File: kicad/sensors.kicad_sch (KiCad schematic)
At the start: 18 parts, among them U10 W25N01GV, U6 ICM-42688-P, U7 BMI270, U8 BMP390, U9 IIS2MDC

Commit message: Gate 1 fixes (crystal gm evidence, LDO output ESR, X7R caps, 50V HF cap, per-MPN datasheets, in_bom flags, project-file merge, parity fields), power re-audit fixes (board-level thermal envelope, USB inrush deviation, R41 VTX 0R link), PCB placement + legalizer + grommet keepouts; Gate 1 reports
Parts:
- C39: value 2.2uF X5R 16V -> 2.2uF X7R 16V; DigiKey 1276-1183-1-ND (verify) -> 1276-1184-1-ND (verify); MPN CL10A225KO8NNNC -> CL10B225KO8NNNC
- C47: value 1uF X5R 25V -> 4.7uF X5R 16V; DigiKey 1276-1102-1-ND (verify) -> 1276-1044-1-ND (verify); MPN CL10A105KA8NNNC -> CL10A475KO8NNNC
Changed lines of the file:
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@@
 			)
 		)
-		(property "Datasheet" "https://product.samsungsem.com/mlcc/"
+		(property "Datasheet" "https://product.samsungsem.com/mlcc/CL05B104KO5NNNC.do"
 			(at 93.98 35.56 0)
 			(effects
@@
 			)
 		)
-		(property "Value" "2.2uF X5R 16V"
+		(property "Value" "2.2uF X7R 16V"
 			(at 119.38 41.91 0)
 			(effects
@@
 			)
 		)
-		(property "Datasheet" "https://product.samsungsem.com/mlcc/"
+		(property "Datasheet" "https://product.samsungsem.com/mlcc/CL10B225KO8NNNC.do"
 			(at 119.38 35.56 0)
 			(effects
@@
 			)
 		)
-		(property "MPN" "CL10A225KO8NNNC"
+		(property "MPN" "CL10B225KO8NNNC"
 			(at 119.38 35.56 0)
 			(effects
@@
 			)
 		)
-		(property "DigiKey" "1276-1183-1-ND (verify)"
+		(property "DigiKey" "1276-1184-1-ND (verify)"
 			(at 119.38 35.56 0)
 			(effects
@@
 			)
 		)
-		(property "Datasheet" "https://product.samsungsem.com/mlcc/"
+		(property "Datasheet" "https://product.samsungsem.com/mlcc/CL05B103KB5NNNC.do"
 			(at 147.32 35.56 0)
 			(effects
@@
 			)
 		)
-		(property "Datasheet" "https://product.samsungsem.com/mlcc/"
+		(property "Datasheet" "https://product.samsungsem.com/mlcc/CL05B104KO5NNNC.do"
 			(at 228.6 35.56 0)
 			(effects
@@
 			)
 		)
-		(property "Datasheet" "https://product.samsungsem.com/mlcc/"
+		(property "Datasheet" "https://product.samsungsem.com/mlcc/CL05B104KO5NNNC.do"
 			(at 254 35.56 0)
 			(effects
@@
 			)
 		)
-		(property "Datasheet" "https://product.samsungsem.com/mlcc/"
+		(property "Datasheet" "https://product.samsungsem.com/mlcc/CL05B104KO5NNNC.do"
 			(at 73.66 71.12 0)
 			(effects
@@
 			)
 		)
-		(property "Datasheet" "https://product.samsungsem.com/mlcc/"
+		(property "Datasheet" "https://product.samsungsem.com/mlcc/CL05B104KO5NNNC.do"
 			(at 93.98 71.12 0)
 			(effects
@@
 			)
 		)
-		(property "Datasheet" "https://product.samsungsem.com/mlcc/"
+		(property "Datasheet" "https://product.samsungsem.com/mlcc/CL05A224KA5NNNC.do"
 			(at 170.18 71.12 0)
 			(effects
@@
 			)
 		)
-		(property "Datasheet" "https://product.samsungsem.com/mlcc/"
+		(property "Datasheet" "https://product.samsungsem.com/mlcc/CL05B104KO5NNNC.do"
 			(at 193.04 71.12 0)
 			(effects
@@
 			)
 		)
-		(property "Value" "1uF X5R 25V"
+		(property "Value" "4.7uF X5R 16V"
 			(at 210.82 77.47 0)
 			(effects
@@
 			)
 		)
-		(property "Datasheet" "https://product.samsungsem.com/mlcc/"
+		(property "Datasheet" "https://product.samsungsem.com/mlcc/CL10A475KO8NNNC.do"
 			(at 210.82 71.12 0)
 			(effects
@@
 			)
 		)
-		(property "MPN" "CL10A105KA8NNNC"
+		(property "MPN" "CL10A475KO8NNNC"
 			(at 210.82 71.12 0)
 			(effects
@@
 			)
 		)
-		(property "DigiKey" "1276-1102-1-ND (verify)"
+		(property "DigiKey" "1276-1044-1-ND (verify)"
 			(at 210.82 71.12 0)
 			(effects
@@
 			)
 		)
-		(property "Datasheet" "https://product.samsungsem.com/mlcc/"
+		(property "Datasheet" "https://product.samsungsem.com/mlcc/CL05B104KO5NNNC.do"
 			(at 22.86 111.76 0)
 			(effects

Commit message: Gate 2 sourcing: apply DigiKey drop-in replacements (G2S-01/02/03/09), PN corrections, regenerate BOM; sourcing report and DigiKey BOM CSVs
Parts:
- C39: value 2.2uF X7R 16V -> 2.2uF X7R 10V; DigiKey 1276-1184-1-ND (verify) -> 1276-1134-1-ND; MPN CL10B225KO8NNNC -> CL10B225KP8NNNC
- C40: DigiKey 1276-1015-1-ND (verify) -> 1276-1028-1-ND
- C45: DigiKey 1276-1255-1-ND (verify) -> 1276-1455-1-ND
- C47: DigiKey 1276-1044-1-ND (verify) -> 1276-1784-1-ND
- U10: MPN W25N01GVZEIG -> W25N01GVZEIG TR
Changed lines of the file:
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@@
 			)
 		)
-		(property "Value" "2.2uF X7R 16V"
+		(property "Value" "2.2uF X7R 10V"
 			(at 119.38 41.91 0)
 			(effects
@@
 			)
 		)
-		(property "Datasheet" "https://product.samsungsem.com/mlcc/CL10B225KO8NNNC.do"
+		(property "Datasheet" "https://product.samsungsem.com/mlcc/CL10B225KP8NNNC.do"
 			(at 119.38 35.56 0)
 			(effects
@@
 			)
 		)
-		(property "MPN" "CL10B225KO8NNNC"
+		(property "MPN" "CL10B225KP8NNNC"
 			(at 119.38 35.56 0)
 			(effects
@@
 			)
 		)
-		(property "DigiKey" "1276-1184-1-ND (verify)"
+		(property "DigiKey" "1276-1134-1-ND"
 			(at 119.38 35.56 0)
 			(effects
@@
 			)
 		)
-		(property "DigiKey" "1276-1015-1-ND (verify)"
+		(property "DigiKey" "1276-1028-1-ND"
 			(at 147.32 35.56 0)
 			(effects
@@
 			)
 		)
-		(property "DigiKey" "1276-1255-1-ND (verify)"
+		(property "DigiKey" "1276-1455-1-ND"
 			(at 170.18 71.12 0)
 			(effects
@@
 			)
 		)
-		(property "DigiKey" "1276-1044-1-ND (verify)"
+		(property "DigiKey" "1276-1784-1-ND"
 			(at 210.82 71.12 0)
 			(effects
@@
 			)
 		)
-		(property "MPN" "W25N01GVZEIG"
+		(property "MPN" "W25N01GVZEIG TR"
 			(at 251.46 71.12 0)
 			(effects

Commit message: Gate 2 re-check: report + fixes (TDK 4.7uF 100V bottom input caps, PNs, BOM regenerated $175.73, inductor keepouts), D-20
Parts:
- U10: DigiKey W25N01GVZEIGCT-ND -> 256-W25N01GVZEIGTRCT-ND
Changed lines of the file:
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@@
 			)
 		)
-		(property "DigiKey" "W25N01GVZEIGCT-ND"
+		(property "DigiKey" "256-W25N01GVZEIGTRCT-ND"
 			(at 251.46 71.12 0)
 			(effects

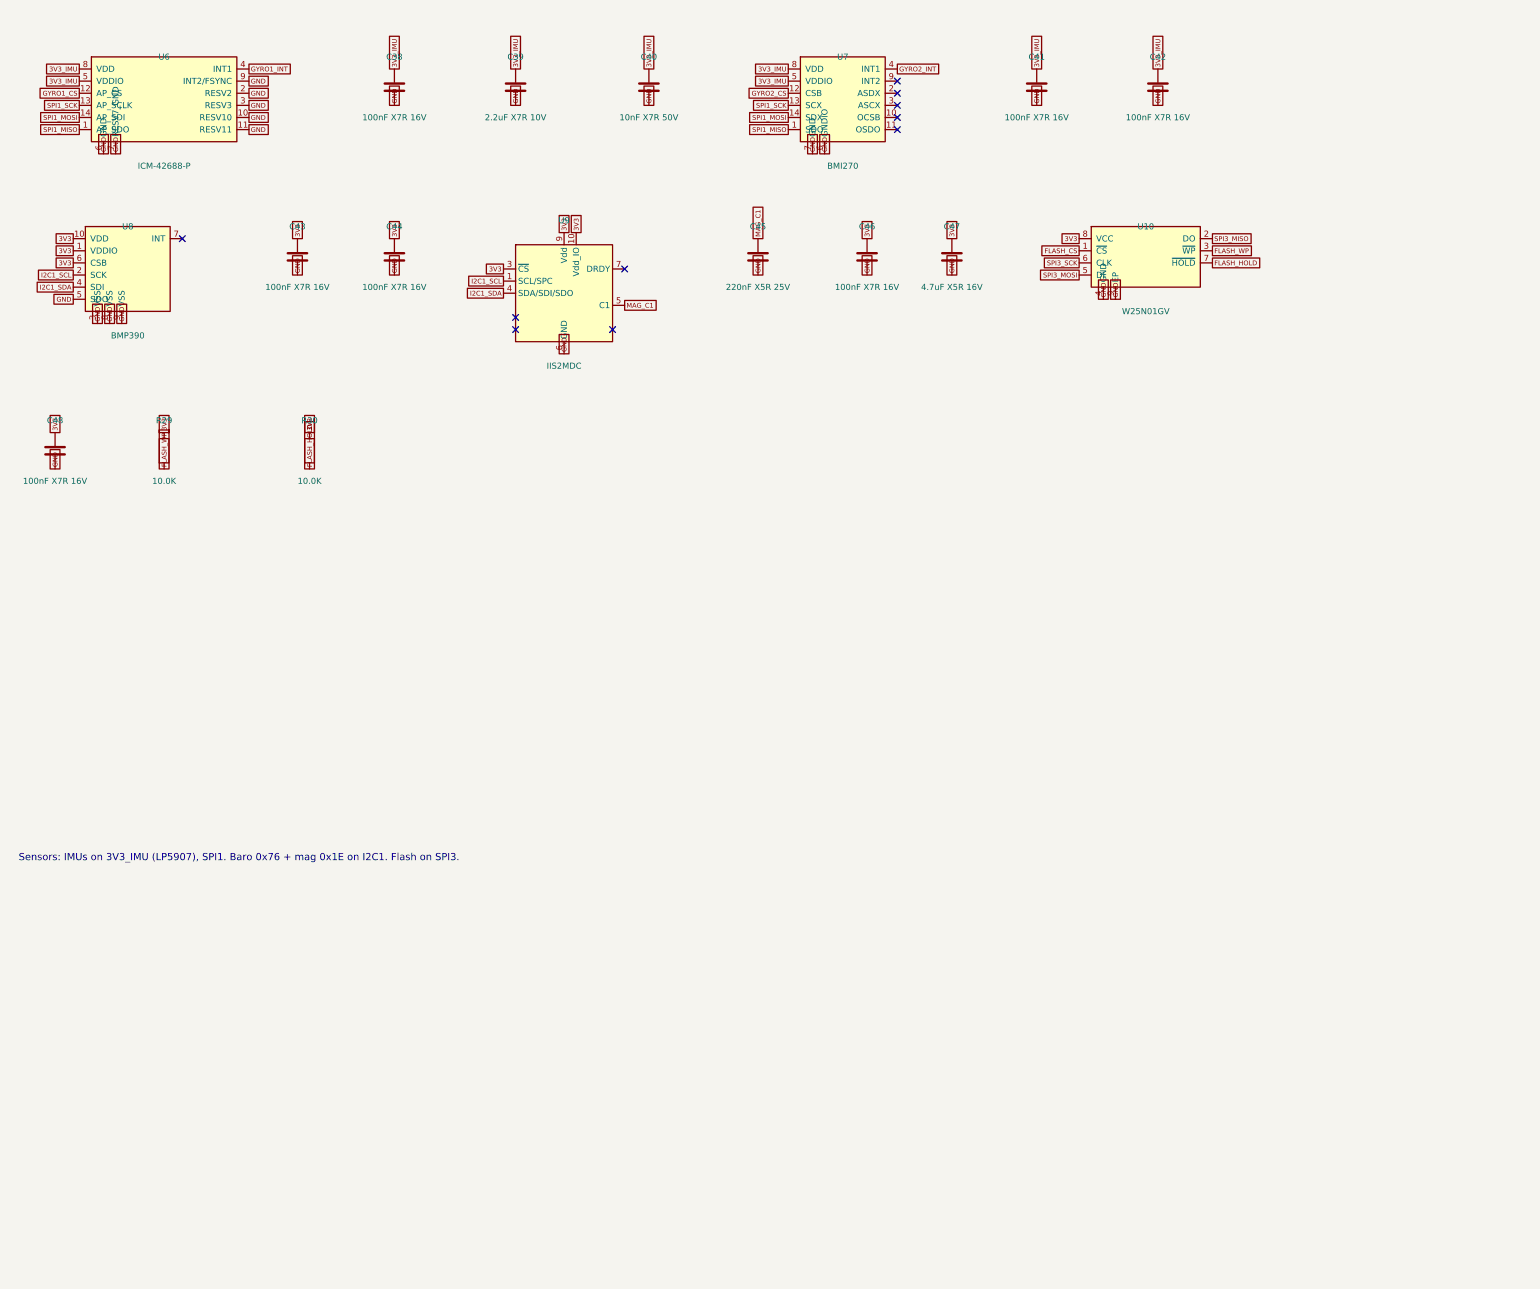
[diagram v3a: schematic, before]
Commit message: Readable schematic: functional blocks with titles, passives wired to their IC pins, GND power symbols, per-rail decoupling banks, labels only between blocks (ERC 0, netcheck OK, same nets)
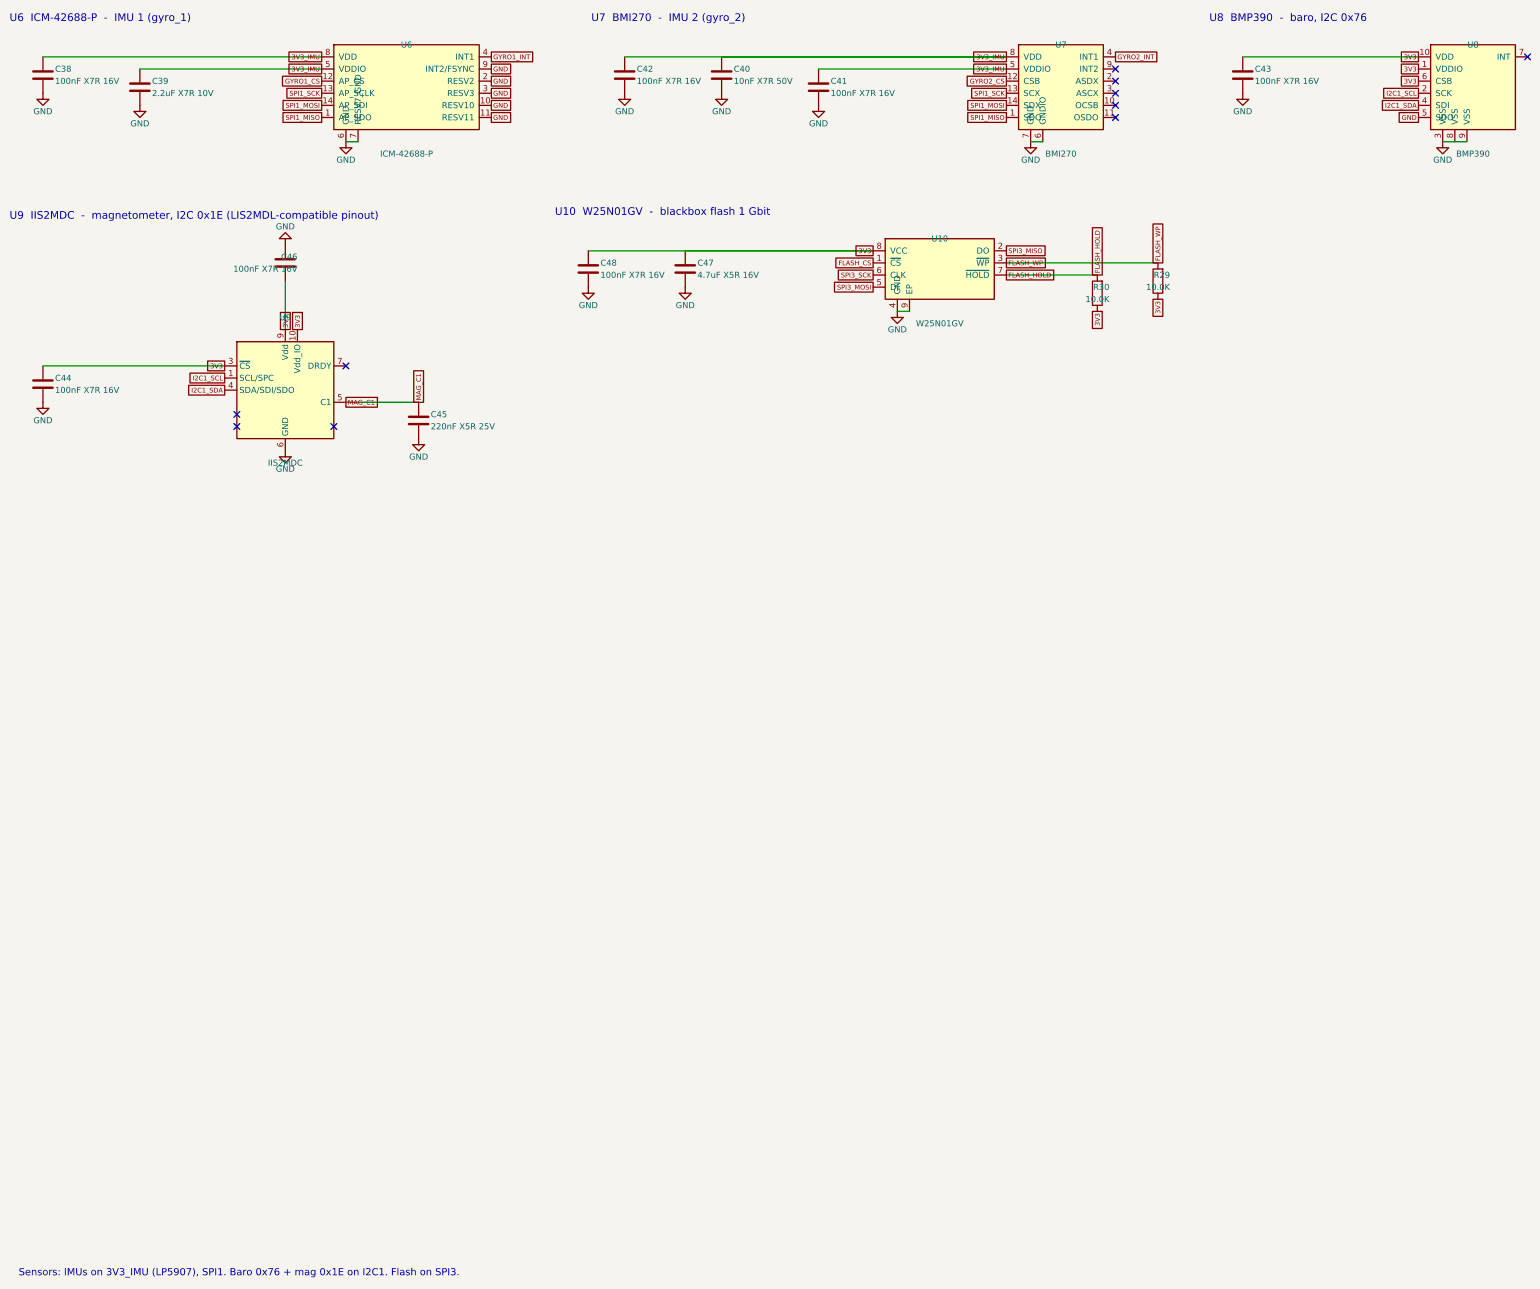
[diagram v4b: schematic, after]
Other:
- note added: "U10 W25N01GV - blackbox flash 1 Gbit"
- note added: "U6 ICM-42688-P - IMU 1 (gyro_1)"
- note added: "U7 BMI270 - IMU 2 (gyro_2)"
- note added: "U8 BMP390 - baro, I2C 0x76"
- note added: "U9 IIS2MDC - magnetometer, I2C 0x1E (LIS2MDL-compatible pinout)"
- moved on the sheet: C38, C39, C40, C41, C42, C43, C44, C45, C46, C47, C48, R29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
